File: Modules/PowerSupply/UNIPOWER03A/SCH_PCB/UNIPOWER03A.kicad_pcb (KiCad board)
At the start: 2 copper layers, 40.1 x 40.1 mm, 32 parts, among them CON1 JACK_DC2.1, J1 CONN1_2, J10 JUMP_2x1, J11 JUMP_2x1, J12 CONN1_1, J13 CONN1_1, J2 CONN1_2, J3 JUMP_2x1, J4 CONN1_2, J5 CONN1_2, J6 CONN1_1, J7 CONN1_1, J8 JUMP_4X2, J9 JUMP_2x1, M1 HOLE, M2 HOLE, M3 HOLE, M4 HOLE, M5 HOLE, M8 HOLE, SW1 Prepinac

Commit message: 
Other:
- rule pad_to_mask_clearance: 0.2 -> 0.12
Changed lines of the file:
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@@
   )
   (setup
-    (last_trace_width 0.8)
+    (last_trace_width 0.3)
     (user_trace_width 0.6)
     (user_trace_width 0.7)
@@
     (pad_size 1.524 1.524)
     (pad_drill 0.762)
-    (pad_to_mask_clearance 0.2)
+    (pad_to_mask_clearance 0.12)
     (aux_axis_origin 0 0)
     (visible_elements 7FFFFF7F)

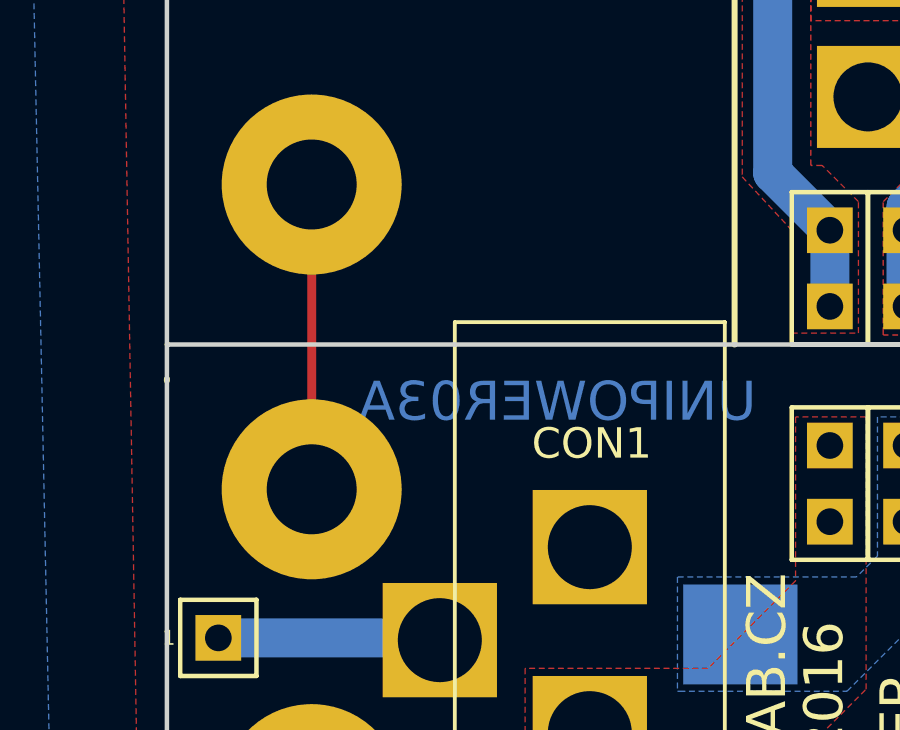
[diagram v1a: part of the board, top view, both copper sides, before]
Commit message: 
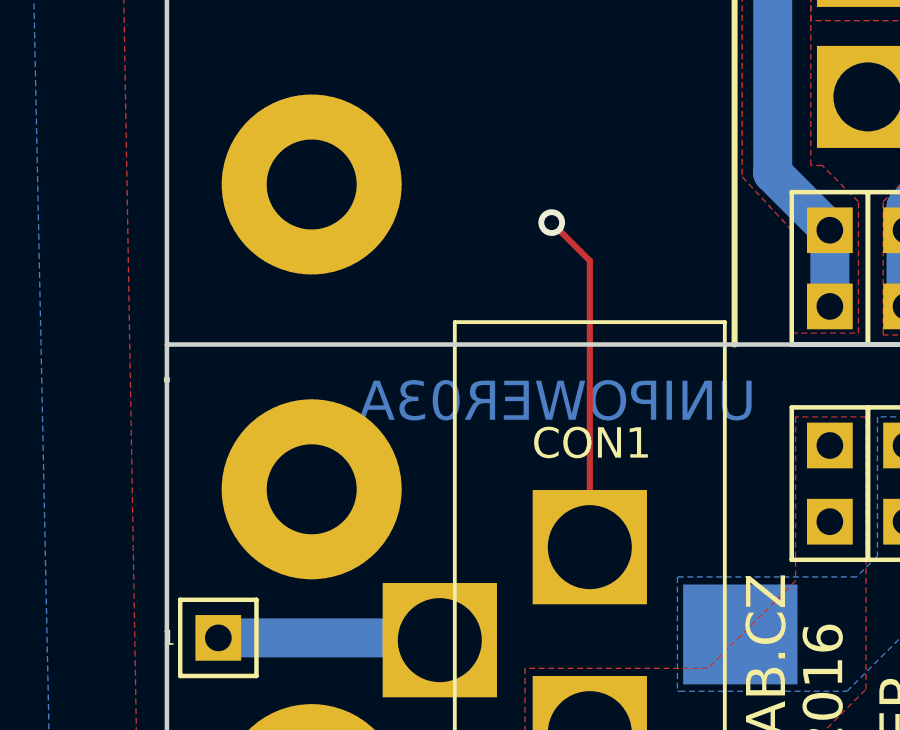
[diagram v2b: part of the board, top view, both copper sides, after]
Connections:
- M1 pad 1: GND -> (no net)
- M2 pad 1: GND -> (no net)
- M3 pad 1: GND -> (no net)
- M4 pad 1: GND -> (no net)
- M5 pad 1: GND -> (no net)
- M8 pad 1: GND -> (no net)
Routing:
- net GND: track 28.7 -> 29.9 mm, vias 0 -> 1
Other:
- net class gnd added: clearance 0.2, trace_width 0.2, via_dia 0.89, via_drill 0.5
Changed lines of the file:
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@@
 (kicad_pcb (version 4) (host pcbnew 4.0.1-stable)
   (general
-    (links 46)
+    (links 40)
     (no_connects 0)
-    (area -4.3815 -43.034 43.736143 1.7695)
+    (area 0.178999 -40.461001 40.461001 -0.178999)
     (thickness 1.6)
     (drawings 14)
-    (tracks 49)
+    (tracks 51)
     (zones 0)
     (modules 32)
@@
     (user_trace_width 1.3)
     (trace_clearance 0.2)
-    (zone_clearance 0.508)
+    (zone_clearance 0.3)
     (zone_45_only no)
     (trace_min 0.2)
@@
     (uvia_dia 0.3)
     (uvia_drill 0.127)
-    (add_net GND)
     (add_net "Net-(CON1-Pad1)")
     (add_net "Net-(CON1-Pad3)")
@@
     (add_net VCC)
   )
+  (net_class gnd ""
+    (clearance 0.2)
+    (trace_width 0.2)
+    (via_dia 0.89)
+    (via_drill 0.5)
+    (uvia_dia 0.3)
+    (uvia_drill 0.127)
+    (add_net GND)
+  )
   (module Mlab_Mechanical:MountingHole_3mm placed (layer F.Cu)
     (at 35.56 -15.24)
@@
     (fp_circle (center 0 0) (end 2.99974 0) (layer Cmts.User) (width 0.381))
     (pad 1 thru_hole circle (at 0 0) (size 6 6) (drill 3) (layers *.Cu *.Adhes *.Mask)
-      (net 1 GND) (clearance 1) (zone_connect 2))
+      (clearance 1) (zone_connect 2))
   )
   (module Mlab_Pin_Headers:Straight_2x04 (layer F.Cu)
@@
     (fp_circle (center 0 0) (end 2.99974 0) (layer Cmts.User) (width 0.381))
     (pad 1 thru_hole circle (at 0 0) (size 6 6) (drill 3) (layers *.Cu *.Adhes *.Mask)
-      (net 1 GND) (clearance 1) (zone_connect 2))
+      (clearance 1) (zone_connect 2))
   )
   (module Mlab_Mechanical:MountingHole_3mm placed (layer F.Cu)
@@
     (fp_circle (center 0 0) (end 2.99974 0) (layer Cmts.User) (width 0.381))
     (pad 1 thru_hole circle (at 0 0) (size 6 6) (drill 3) (layers *.Cu *.Adhes *.Mask)
-      (net 1 GND) (clearance 1) (zone_connect 2))
+      (clearance 1) (zone_connect 2))
   )
   (module Mlab_Mechanical:MountingHole_3mm placed (layer F.Cu)
@@
     (fp_circle (center 0 0) (end 2.99974 0) (layer Cmts.User) (width 0.381))
     (pad 1 thru_hole circle (at 0 0) (size 6 6) (drill 3) (layers *.Cu *.Adhes *.Mask)
-      (net 1 GND) (clearance 1) (zone_connect 2))
+      (clearance 1) (zone_connect 2))
   )
   (module Mlab_Mechanical:MountingHole_3mm placed (layer F.Cu)
@@
     (fp_circle (center 0 0) (end 2.99974 0) (layer Cmts.User) (width 0.381))
     (pad 1 thru_hole circle (at 0 0) (size 6 6) (drill 3) (layers *.Cu *.Adhes *.Mask)
-      (net 1 GND) (clearance 1) (zone_connect 2))
+      (clearance 1) (zone_connect 2))
   )
   (module Mlab_Mechanical:MountingHole_3mm placed (layer F.Cu)
@@
     (fp_circle (center 0 0) (end 2.99974 0) (layer Cmts.User) (width 0.381))
     (pad 1 thru_hole circle (at 0 0) (size 6 6) (drill 3) (layers *.Cu *.Adhes *.Mask)
-      (net 1 GND) (clearance 1) (zone_connect 2))
+      (clearance 1) (zone_connect 2))
   )
   (module Mlab_Pin_Headers:Straight_1x01 (layer F.Cu)
@@
   (gr_line (start 40.386 -0.254) (end 40.386 -40.386) (angle 90) (layer Edge.Cuts) (width 0.15))
   (gr_line (start 0.254 -0.254) (end 40.386 -0.254) (angle 90) (layer Edge.Cuts) (width 0.15))
-  (segment (start 5.08 -15.24) (end 5.08 -25.4) (width 0.3) (layer F.Cu) (net 1))
+  (segment (start 14.351 -13.312) (end 14.351 -22.86) (width 0.2) (layer F.Cu) (net 1))
+  (segment (start 14.351 -22.86) (end 13.081 -24.13) (width 0.2) (layer F.Cu) (net 1))
+  (via (at 13.081 -24.13) (size 0.89) (drill 0.5) (layers F.Cu B.Cu) (net 1))
   (segment (start 27.432 -16.7005) (end 27.432 -21.336) (width 1.3) (layer F.Cu) (net 1))
   (segment (start 28.067 -32.512) (end 28.067 -37.465) (width 0.8) (layer F.Cu) (net 1))
@@
   )
   (zone (net 1) (net_name GND) (layer F.Cu) (hatch edge 0.508)
-    (connect_pads yes (clearance 0.508))
+    (connect_pads yes (clearance 0.3))
     (min_thickness 0.254)
     (fill yes (arc_segments 16) (thermal_gap 0.508) (thermal_bridge_width 0.508))
@@
   )
   (zone (net 1) (net_name GND) (layer B.Cu) (hatch edge 0.508)
-    (connect_pads yes (clearance 0.508))
+    (connect_pads yes (clearance 0.3))
     (min_thickness 0.254)
     (fill yes (arc_segments 16) (thermal_gap 0.508) (thermal_bridge_width 0.508))

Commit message: Nahrani dokumentace
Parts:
- D1, D2: value LED -> RED
- D3: value LED -> GREEN
- D4: value D -> M4
- D5: value LED -> ORANGE
- F1: value F_Small -> 1,1A
- FI1: value EMI_FILTER -> NFM21PC105
- R1, R2, R3, R4: value R -> 2k2
- SW1: value Prepinac -> SL19121
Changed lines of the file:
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@@
       (effects (font (size 1 1) (thickness 0.15)) (justify mirror))
     )
-    (fp_text value EMI_FILTER (at 2.794 -1.905) (layer B.SilkS) hide
+    (fp_text value NFM21PC105 (at 2.794 -1.905) (layer B.SilkS) hide
       (effects (font (size 1 1) (thickness 0.15)) (justify mirror))
     )
@@
       (effects (font (size 0.50038 0.50038) (thickness 0.10922)))
     )
-    (fp_text value R (at 0.127 0.381 180) (layer F.SilkS) hide
+    (fp_text value 2k2 (at 0.127 0.381 180) (layer F.SilkS) hide
       (effects (font (size 0.50038 0.50038) (thickness 0.10922)))
     )
@@
       (effects (font (size 0.50038 0.50038) (thickness 0.10922)))
     )
-    (fp_text value R (at 0.0635 -1.3335 180) (layer F.SilkS) hide
+    (fp_text value 2k2 (at 0.0635 -1.3335 180) (layer F.SilkS) hide
       (effects (font (size 0.50038 0.50038) (thickness 0.10922)))
     )
@@
       (effects (font (size 0.50038 0.50038) (thickness 0.10922)))
     )
-    (fp_text value R (at 0.127 0.381 180) (layer F.SilkS) hide
+    (fp_text value 2k2 (at 0.127 0.381 180) (layer F.SilkS) hide
       (effects (font (size 0.50038 0.50038) (thickness 0.10922)))
     )
@@
       (effects (font (size 1.016 1.016) (thickness 0.2032)) (justify mirror))
     )
-    (fp_text value Prepinac (at -4.5593 0.2667 450) (layer B.SilkS) hide
+    (fp_text value SL19121 (at -4.5593 0.2667 450) (layer B.SilkS) hide
       (effects (font (size 1.016 1.016) (thickness 0.2032)) (justify mirror))
     )
@@
       (effects (font (size 0.50038 0.50038) (thickness 0.10922)))
     )
-    (fp_text value R (at 0.0635 1.397 180) (layer F.SilkS) hide
+    (fp_text value 2k2 (at 0.0635 1.397 180) (layer F.SilkS) hide
       (effects (font (size 0.50038 0.50038) (thickness 0.10922)))
     )
@@
       (effects (font (thickness 0.3048)))
     )
-    (fp_text value LED (at 0 3.81 180) (layer F.SilkS) hide
+    (fp_text value RED (at 0 3.81 180) (layer F.SilkS) hide
       (effects (font (thickness 0.3048)))
     )
@@
       (effects (font (thickness 0.3048)))
     )
-    (fp_text value LED (at 0 3.81 180) (layer F.SilkS) hide
+    (fp_text value RED (at 0 3.81 180) (layer F.SilkS) hide
       (effects (font (thickness 0.3048)))
     )
@@
       (effects (font (thickness 0.3048)))
     )
-    (fp_text value LED (at 0 3.81 180) (layer F.SilkS) hide
+    (fp_text value GREEN (at 0 3.81 180) (layer F.SilkS) hide
       (effects (font (thickness 0.3048)))
     )
@@
       (effects (font (thickness 0.3048)) (justify mirror))
     )
-    (fp_text value D (at 0 -3.81) (layer B.SilkS) hide
+    (fp_text value M4 (at 0 -3.81) (layer B.SilkS) hide
       (effects (font (thickness 0.3048)) (justify mirror))
     )
@@
       (effects (font (thickness 0.3048)))
     )
-    (fp_text value LED (at 0 3.81 180) (layer F.SilkS) hide
+    (fp_text value ORANGE (at 0 3.81 180) (layer F.SilkS) hide
       (effects (font (thickness 0.3048)))
     )
@@
       (effects (font (thickness 0.3048)) (justify mirror))
     )
-    (fp_text value F_Small (at 0 -3.81 270) (layer B.SilkS) hide
+    (fp_text value 1,1A (at 0 -3.81 270) (layer B.SilkS) hide
       (effects (font (thickness 0.3048)) (justify mirror))
     )
